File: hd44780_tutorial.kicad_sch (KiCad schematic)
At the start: 28 parts, among them J1 LCD_2004_PinSocket_1x16_P2.54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, J2 USB4105-GF-A, SW1 REG SELECT, SW2 ENABLE, SW3 DS02C-254-1L-08BE

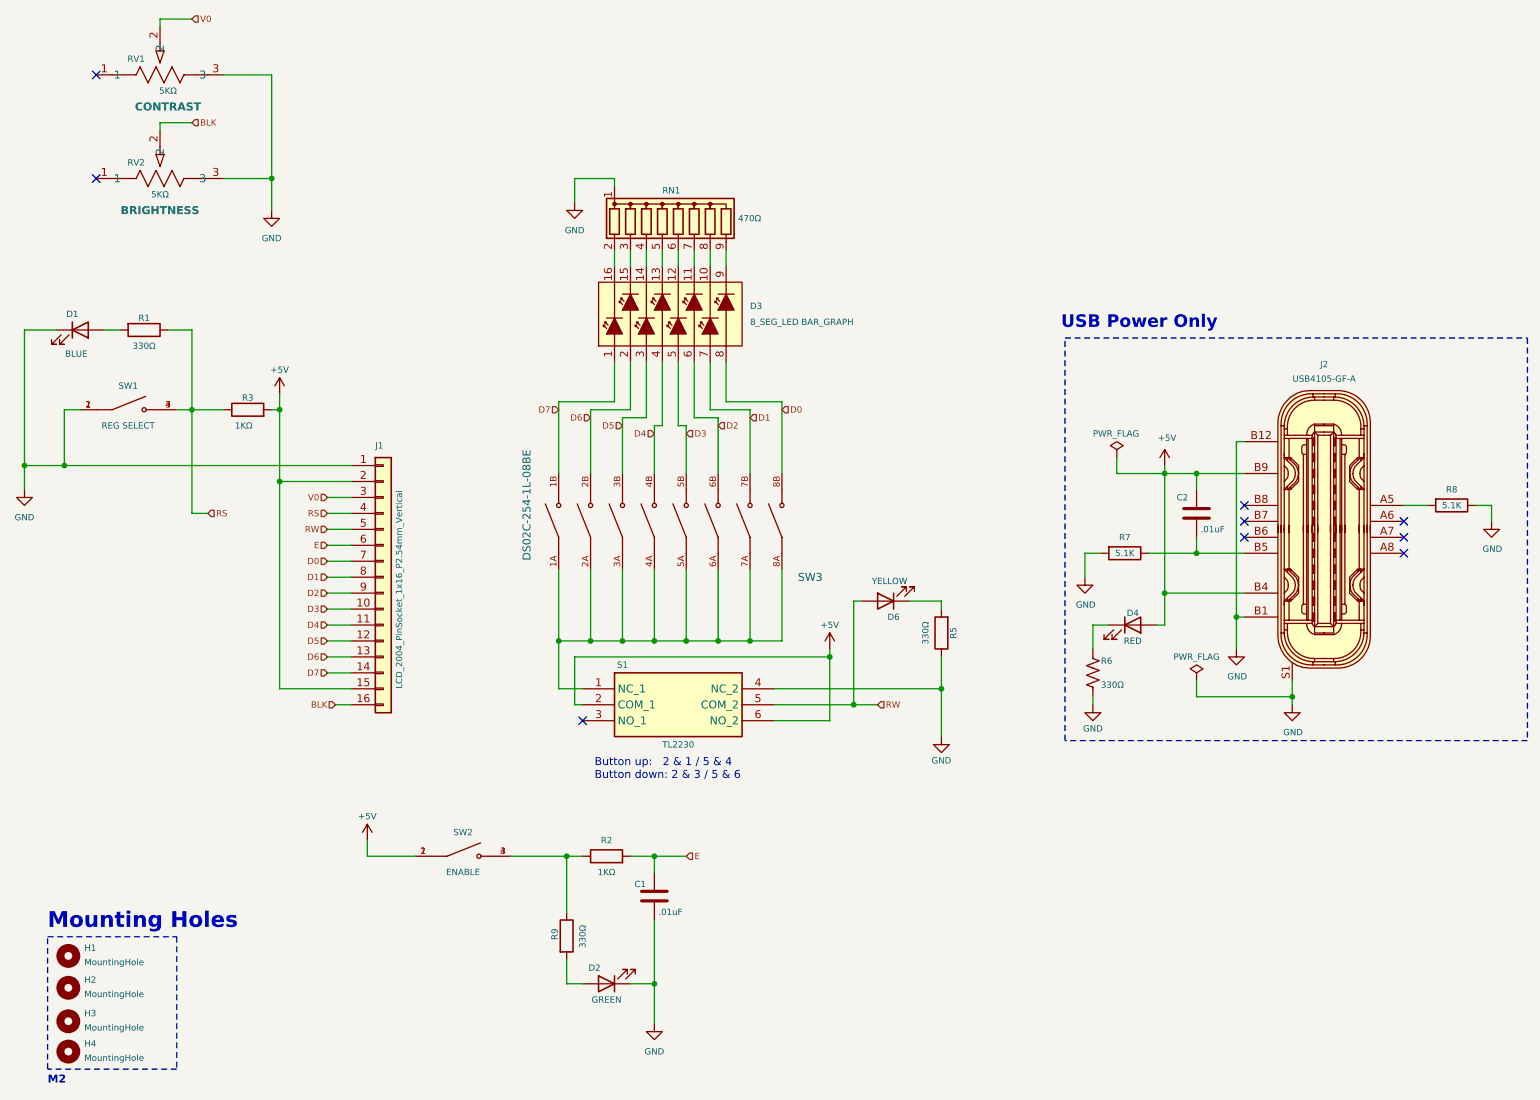
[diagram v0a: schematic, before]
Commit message: Tried a new USB-C port and hate it. Prfeparing to revert to get rid of it.
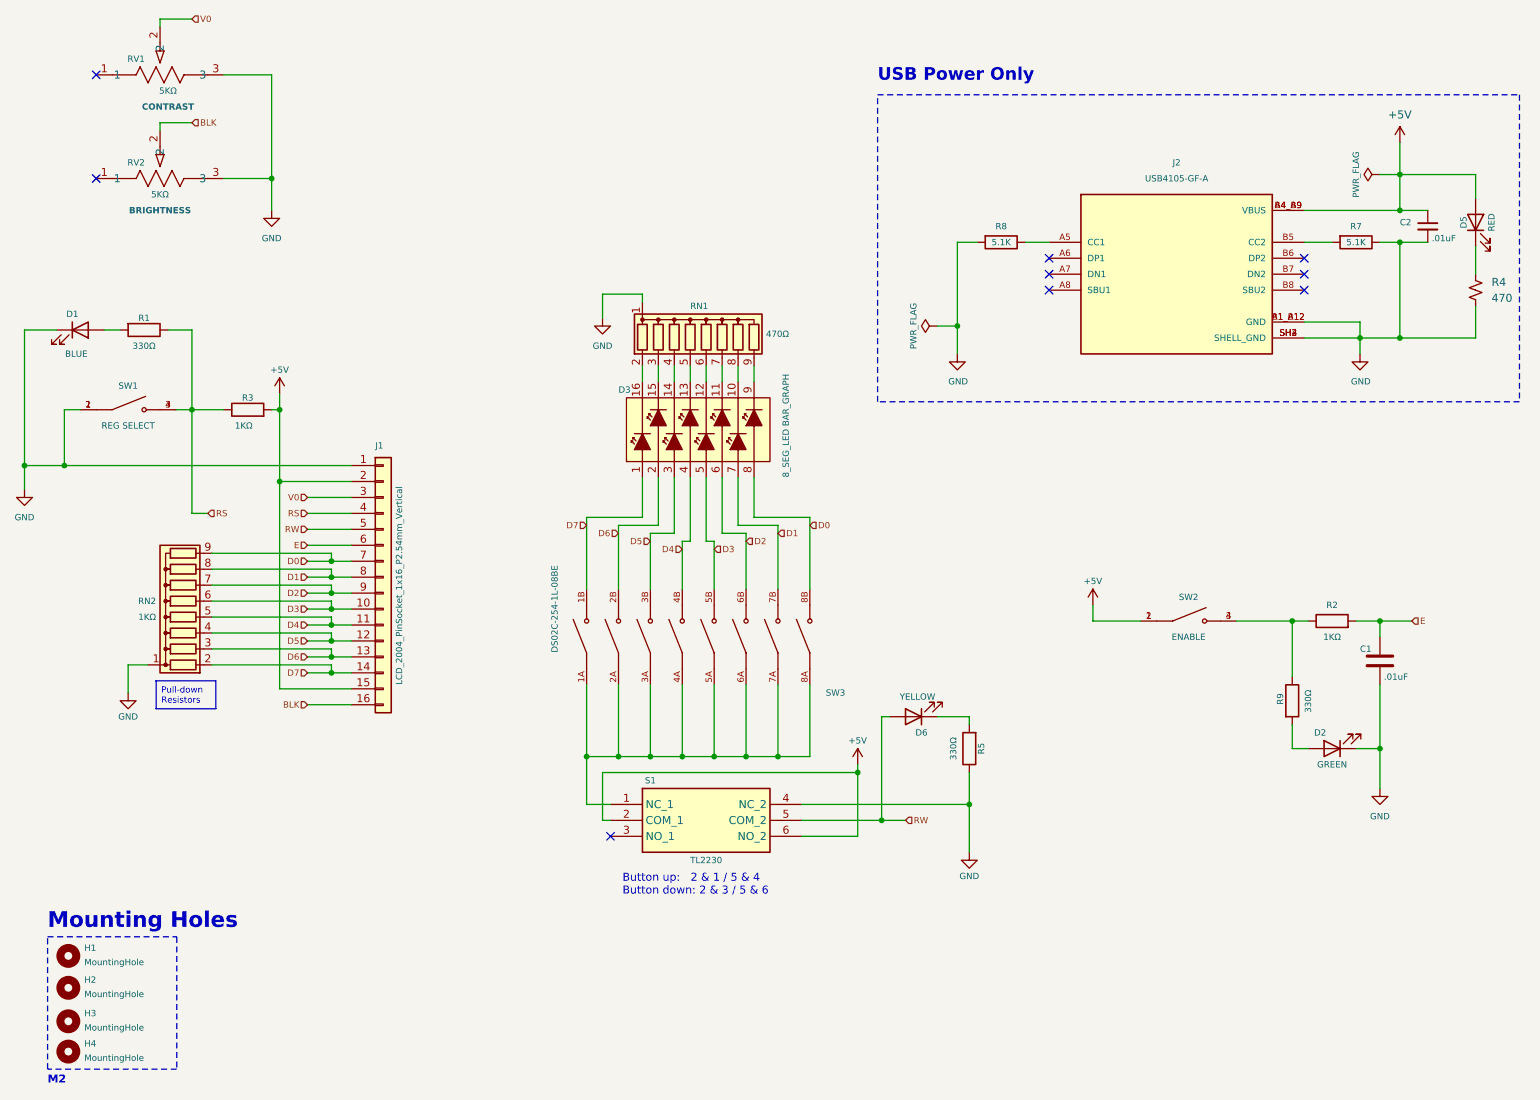
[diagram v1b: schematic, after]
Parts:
- removed C2: .01uF, Capacitor_THT:C_Disc_D4.7mm_W2.5mm_P5.00mm, symbol Device:C
- removed D4: RED, LED_THT:LED_D3.0mm, symbol Device:LED
- removed R6: 330Ω, Resistor_THT:R_Axial_DIN0207_L6.3mm_D2.5mm_P7.62mm_Horizontal, symbol Device:R_US
- added C2: .01uF, Capacitor_THT:C_Disc_D4.7mm_W2.5mm_P5.00mm, symbol Device:C_Small
- added D5: RED, LED_THT:LED_D3.0mm, symbol Device:LED
- added R4: 470, Resistor_THT:R_Axial_DIN0207_L6.3mm_D2.5mm_P7.62mm_Horizontal, symbol Device:R_Small_US
- added RN2: 1KΩ, footprints:R_Array_SIP9, symbol hd44780_tutorial:R_Network08
- J2: footprint footprints:USB_C_Receptacle_HRO_TYPE-C-31-M-12 -> footprints:GCT_USB4105-GF-A; DK_Datasheet_Link https://media.digikey.com/pdf/Data%20Sheets/GCT%20PDFs/USB4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 -> (none); DK_Detail_Page https://www.digikey.com/en/products/detail/gct/USB4105-GF-A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 -> (none); Digi-Key_PN 2073-USB4105-GF-ATR-ND -> (none); MANUFACTURER (none) -> GCT; MAXIMUM_PACKAGE_HEIGHT (none) -> 3.31 mm; MPN USB4105-GF-A -> (none); Manufacturer GCT -> (none); PARTREV (none) -> A3; STANDARD (none) -> Manufacturer Recommendations
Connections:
- net +5V: now also J2.A4_B9 (VBUS), J2.B4_A9 (VBUS), C2.1, D5.2 (A); no longer J2.A4, J2.A9, J2.B4, J2.B9
- net D0: now also RN2.9 (R8)
- net D1: now also RN2.8 (R7)
- net D2: now also RN2.7 (R6)
- net D3: now also RN2.6 (R5)
- net D4: now also RN2.5 (R4)
- net D5: now also RN2.4 (R3)
- net D6: now also RN2.3 (R2)
- net D7: now also RN2.2 (R1)
- net GND: now also J2.A1_B12 (GND), J2.B1_A12 (GND), J2.SH1 (SHELL_GND), J2.SH2 (SHELL_GND), J2.SH3 (SHELL_GND), J2.SH4 (SHELL_GND), R7.1, R8.2, C2.2, R4.2, RN2.1 (common); no longer J2.A1, J2.A12, J2.B1, J2.B12, J2.S1, R7.2, R8.1
- net at J2.B5 (CC2): now also R7.2; no longer R7.1
- net at J2.A5 (CC1): now also R8.1; no longer R8.2
- new net: D5.1 (K), R4.1
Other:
- moved on the sheet: C1, D2, D3, D6, R2, R5, R9, RN1, S1, SW2, SW3

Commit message: Revert "Tried a new USB-C port and hate it. Prfeparing to revert to get rid of it."
This reverts commit 31f363ccd091cdbcf9bc00afb548c8c72483716e.
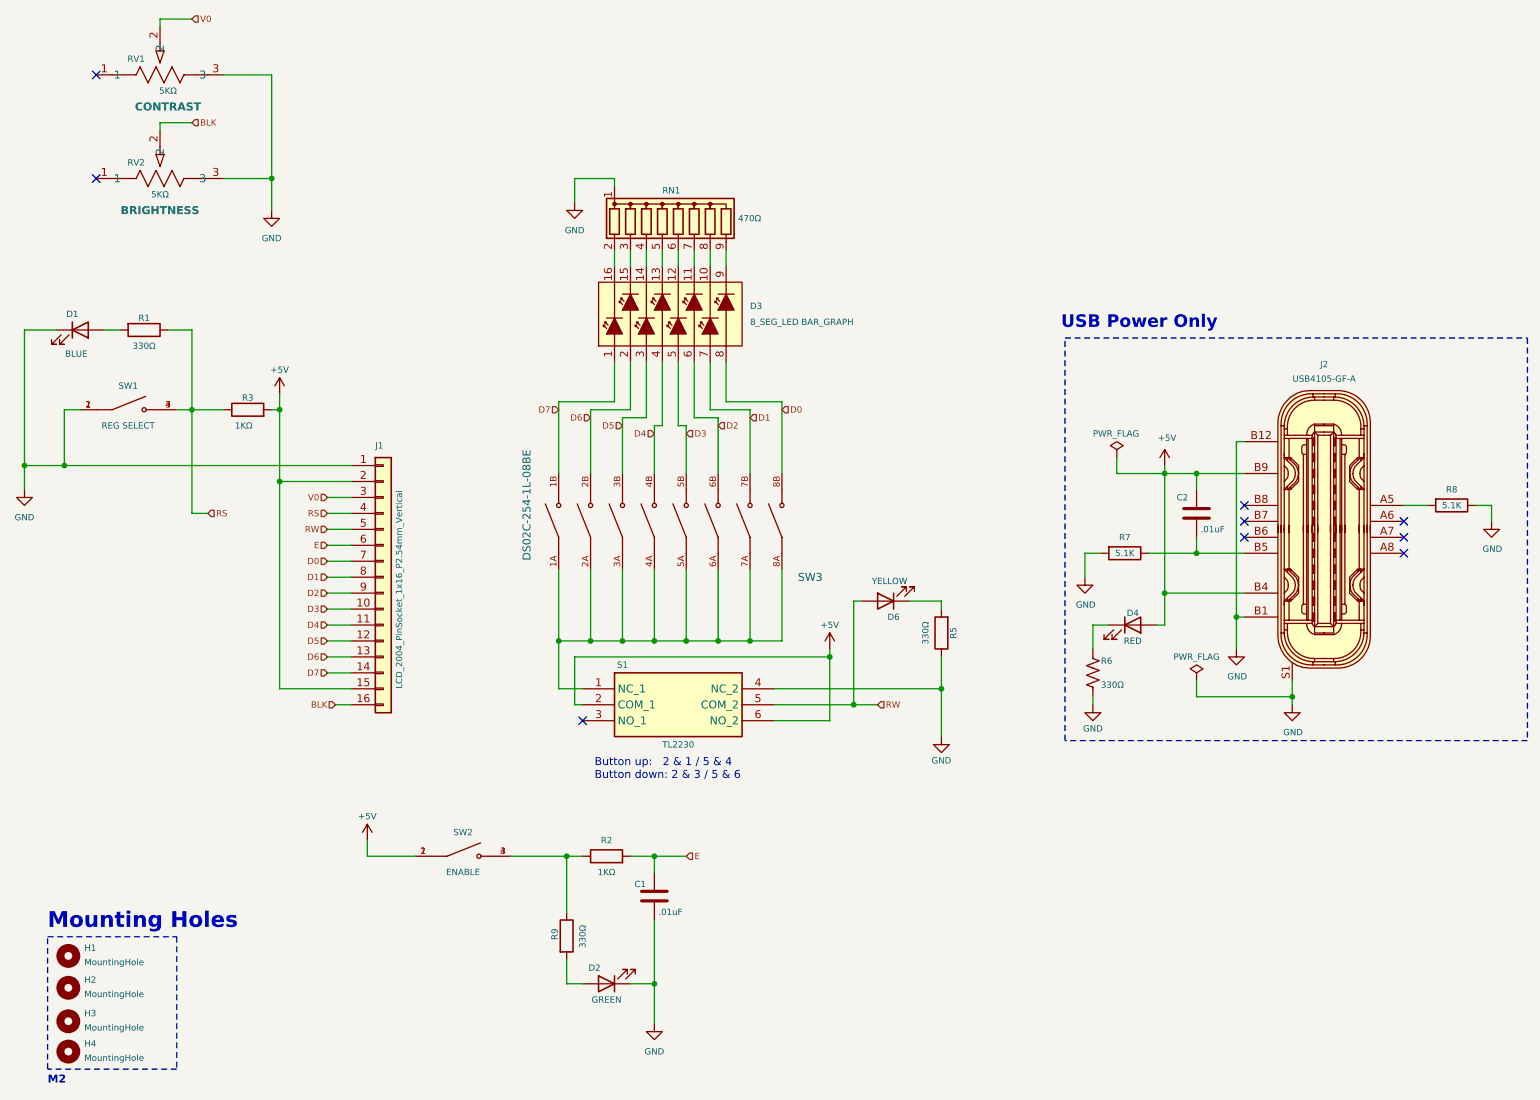
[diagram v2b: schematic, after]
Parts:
- removed C2: .01uF, Capacitor_THT:C_Disc_D4.7mm_W2.5mm_P5.00mm, symbol Device:C_Small
- removed D5: RED, LED_THT:LED_D3.0mm, symbol Device:LED
- removed R4: 470, Resistor_THT:R_Axial_DIN0207_L6.3mm_D2.5mm_P7.62mm_Horizontal, symbol Device:R_Small_US
- removed RN2: 1KΩ, footprints:R_Array_SIP9, symbol hd44780_tutorial:R_Network08
- added C2: .01uF, Capacitor_THT:C_Disc_D4.7mm_W2.5mm_P5.00mm, symbol Device:C
- added D4: RED, LED_THT:LED_D3.0mm, symbol Device:LED
- added R6: 330Ω, Resistor_THT:R_Axial_DIN0207_L6.3mm_D2.5mm_P7.62mm_Horizontal, symbol Device:R_US
- J2: footprint footprints:GCT_USB4105-GF-A -> footprints:USB_C_Receptacle_HRO_TYPE-C-31-M-12; DK_Datasheet_Link (none) -> https://media.digikey.com/pdf/Data%20Sheets/GCT%20PDFs/USB4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; DK_Detail_Page (none) -> https://www.digikey.com/en/products/detail/gct/USB4105-GF-A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; Digi-Key_PN (none) -> 2073-USB4105-GF-ATR-ND; MANUFACTURER GCT -> (none); MAXIMUM_PACKAGE_HEIGHT 3.31 mm -> (none); MPN (none) -> USB4105-GF-A; Manufacturer (none) -> GCT; PARTREV A3 -> (none); STANDARD Manufacturer Recommendations -> (none)
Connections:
- net +5V: now also J2.A4, J2.A9, J2.B4, J2.B9, C2.1, D4.2 (A); no longer J2.A4_B9 (VBUS), J2.B4_A9 (VBUS)
- net GND: now also J2.A1, J2.A12, J2.B1, J2.B12, J2.S1, R7.2, R8.1, R6.1; no longer J2.A1_B12 (GND), J2.B1_A12 (GND), J2.SH1 (SHELL_GND), J2.SH2 (SHELL_GND), J2.SH3 (SHELL_GND), J2.SH4 (SHELL_GND), R7.1, R8.2
- net at J2.A5: now also R8.2; no longer R8.1
- net at J2.B5: now also R7.1, C2.2; no longer R7.2
- new net: D4.1 (K), R6.2
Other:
- moved on the sheet: C1, D2, D3, D6, R2, R5, R9, RN1, S1, SW2, SW3
